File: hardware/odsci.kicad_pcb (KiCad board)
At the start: 4 copper layers, 50 x 69.2 mm, 29 parts, among them J1 USB_C_Receptacle, J2 Conn_01x03_Pin, J3 Conn_01x04_Pin, J4 Screw_Terminal_01x03, SW1 SW_Push, U1 TPS7A4701xRGW, U2 STM32F042K6Tx, U3 USBLC6-2SC6

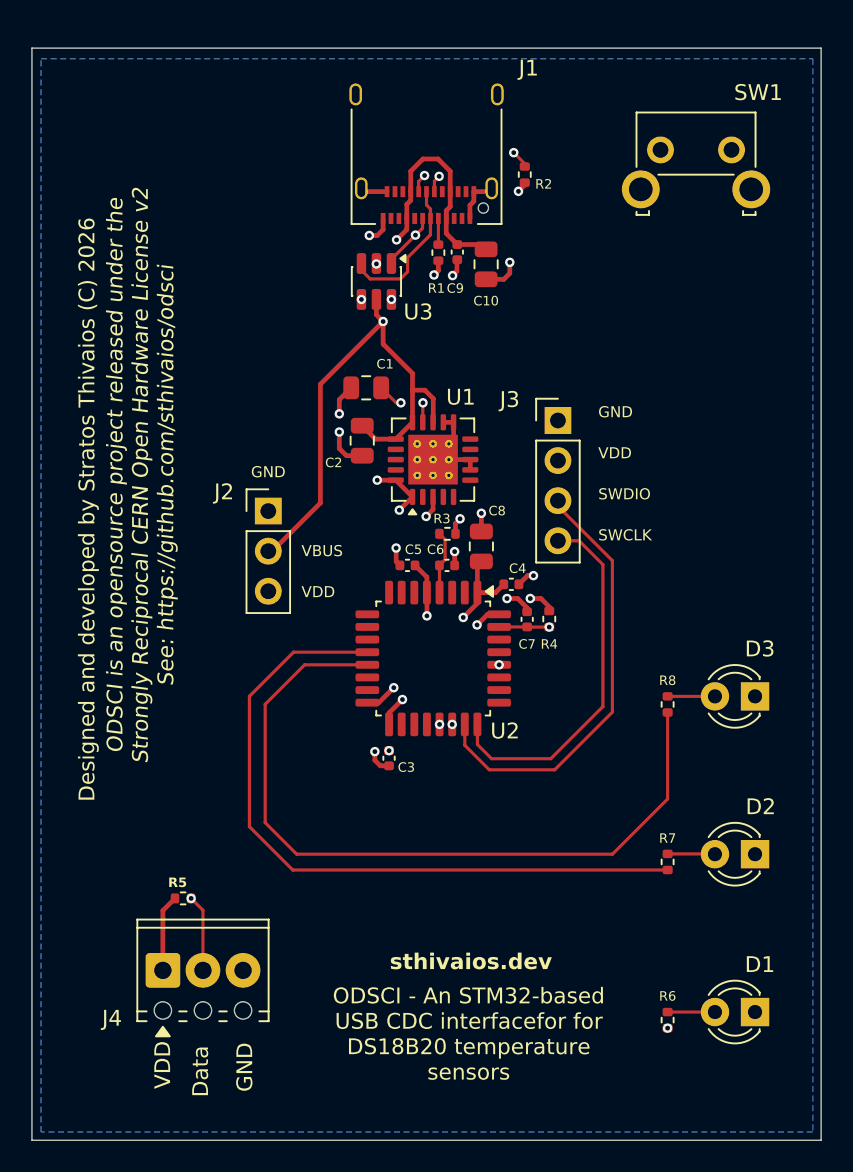
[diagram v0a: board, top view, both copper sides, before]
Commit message: hardware: add mounting holes to pcb
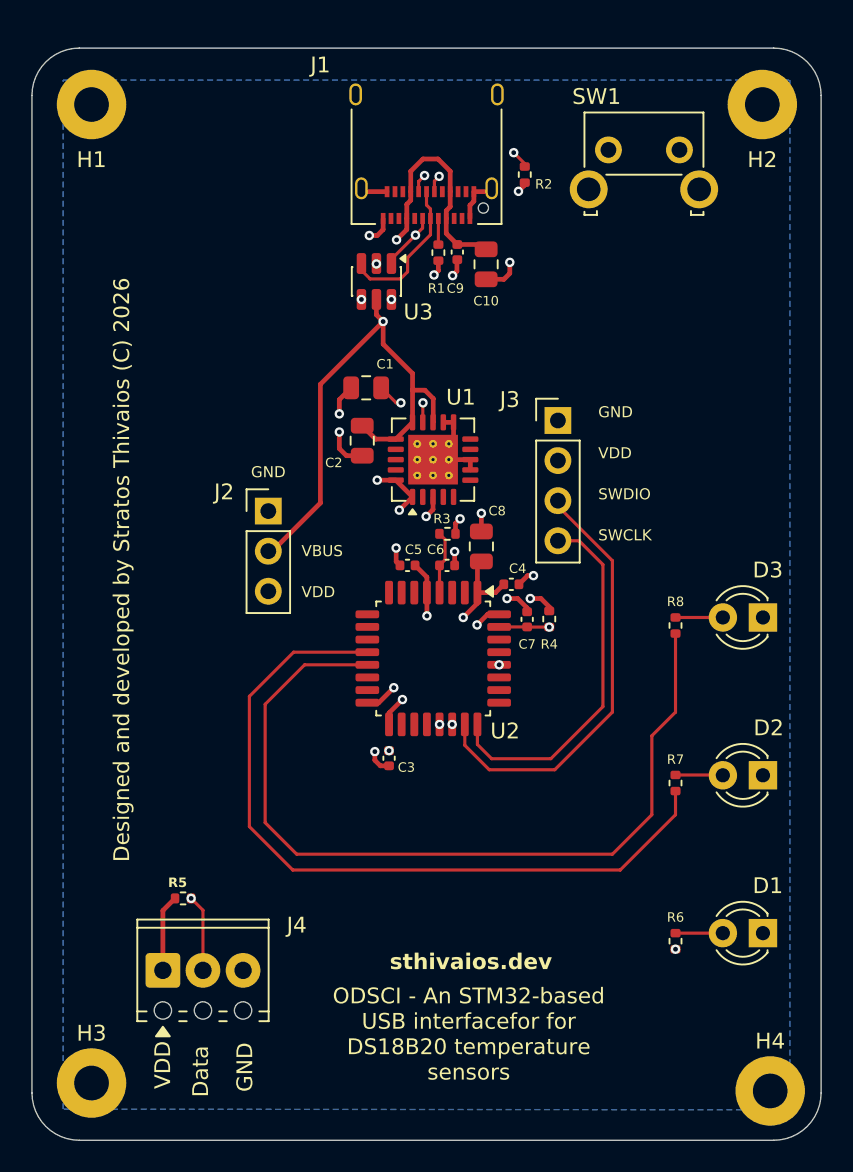
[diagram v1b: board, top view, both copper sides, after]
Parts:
- added H1: MountingHole_Pad, MountingHole:MountingHole_2.2mm_M2_Pad, F.Cu at (129.5, 75.5)
- added H2: MountingHole_Pad, MountingHole:MountingHole_2.2mm_M2_Pad, F.Cu at (172.0, 75.5)
- added H3: MountingHole_Pad, MountingHole:MountingHole_2.2mm_M2_Pad, F.Cu at (129.5, 137.5)
- added H4: MountingHole_Pad, MountingHole:MountingHole_2.2mm_M2_Pad, F.Cu at (172.5, 138.0)
- moved D1 5.02 mm to (172.0, 128.0)
- moved D2 5.02 mm to (172.0, 118.0)
- moved D3 5.02 mm to (172.0, 108.0)
- moved R6 5.02 mm to (166.5, 128.5)
- moved R7 5.02 mm to (166.5, 118.5)
- moved R8 5.02 mm to (166.5, 108.5)
- moved SW1 3.30 mm to (162.2, 78.4)
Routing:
- net CAPTURE_LED: track 48.3 -> 53.5 mm
- net ACTIVITY_LED: track 44.5 -> 48.0 mm
- net Net-(U2-PB8): track 38.2 -> 36.8 mm
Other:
- outline, holes or cut-outs redrawn
- board text added: "ODSCI - An STM32-based USB interfacefor for DS18B20 temperature sensors"
- board text removed: "ODSCI - An STM32-based USB CDC interfacefor for DS18B20 temperature sensors"
- board text removed: "ODSCI is an opensource project released under the Strongly Reciprocal CERN Open Hardware License v2 See: https://github.com/sthivaios/odsci"

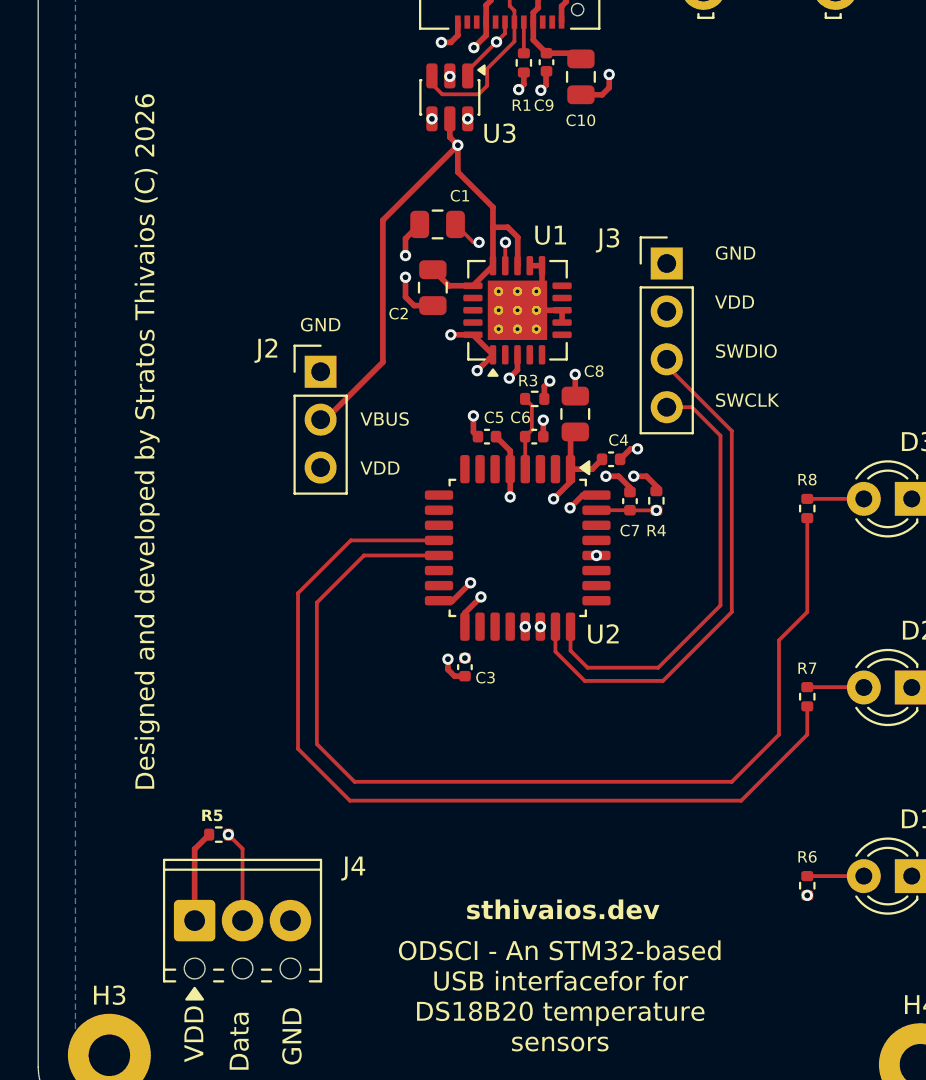
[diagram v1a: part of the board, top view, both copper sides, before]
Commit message: hardware: add a few decoupling caps
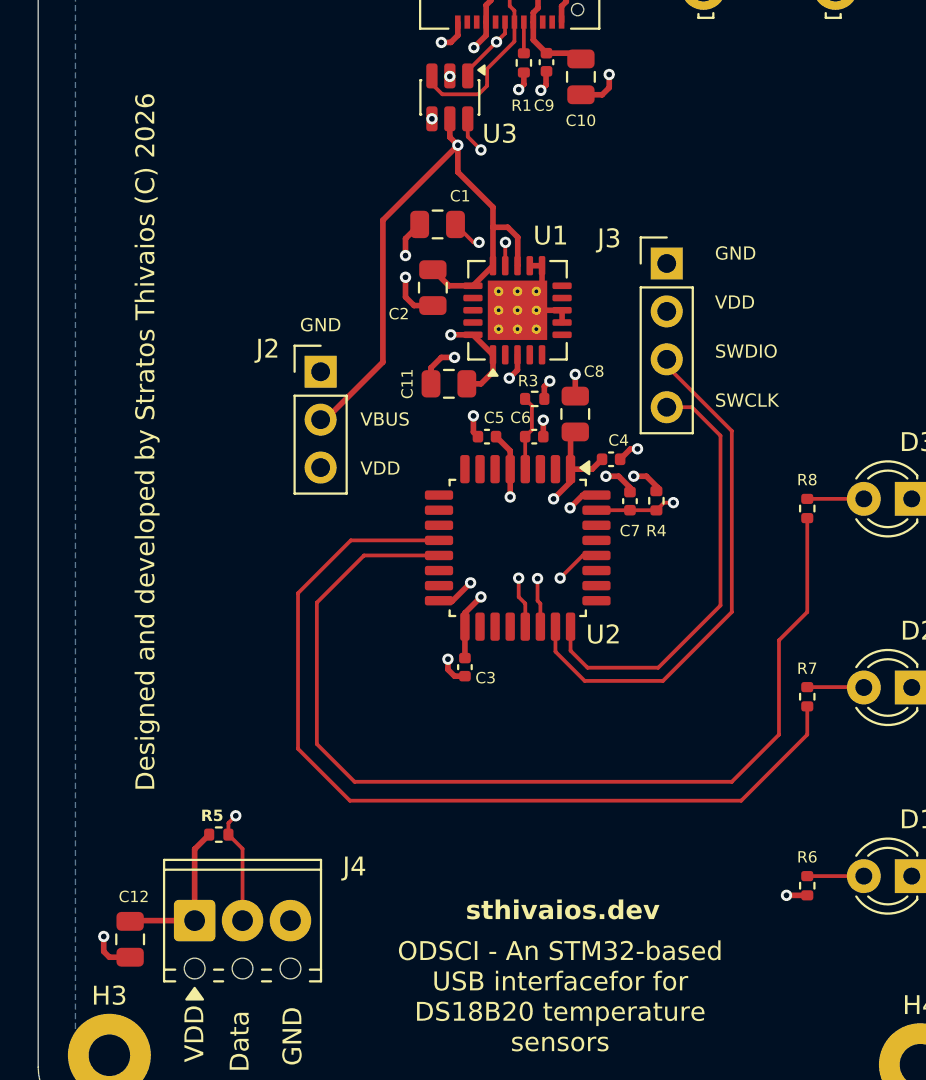
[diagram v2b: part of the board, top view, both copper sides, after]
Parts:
- added C11: 47uF, Capacitor_SMD:C_0805_2012Metric, F.Cu at (147.5, 101.9)
- added C12: 4.7uF, Capacitor_SMD:C_0805_2012Metric, F.Cu at (130.6, 131.3)
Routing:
- net VDD: track 23.1 -> 30.8 mm, vias 9 -> 7
- net GND: track 33.6 -> 38.3 mm, vias 17 -> 19
- net ONEWIRE_BUS: track 34.3 -> 37.8 mm
- net USB_D_POSITIVE: track 35.0 -> 35.6 mm
- net USB_D_NEGATIVE: track 31.9 -> 32.5 mm

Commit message: hardware: layout of pcb
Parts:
- moved C12 60.7 mm to (191.0, 125.8)
- moved J4 60.7 mm to (194.5, 124.8)
- moved R5 60.7 mm to (195.7, 120.2)
- moved H3 58.6 mm to (187.6, 130.1)
- moved H1 58.5 mm to (187.8, 70.2)
- moved C1 57.3 mm to (203.8, 86.6)
- moved C10 57.3 mm to (211.4, 78.8)
- moved C11 57.3 mm to (204.4, 95.1)
- moved C2 57.3 mm to (203.6, 90.0)
- moved C3 57.3 mm to (205.3, 110.1)
- moved C4 57.3 mm to (213.0, 99.1)
- moved C5 57.3 mm to (206.4, 97.9)
- moved C6 57.3 mm to (208.9, 97.9)
- moved C7 57.3 mm to (214.0, 101.3)
- moved C8 57.3 mm to (211.1, 96.7)
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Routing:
- net ONEWIRE_BUS: track 37.8 -> 34.0 mm
- net Net-(U2-PB8): track 37.1 -> 35.6 mm
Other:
- board size 50 x 69.2 mm -> 50 x 70 mm

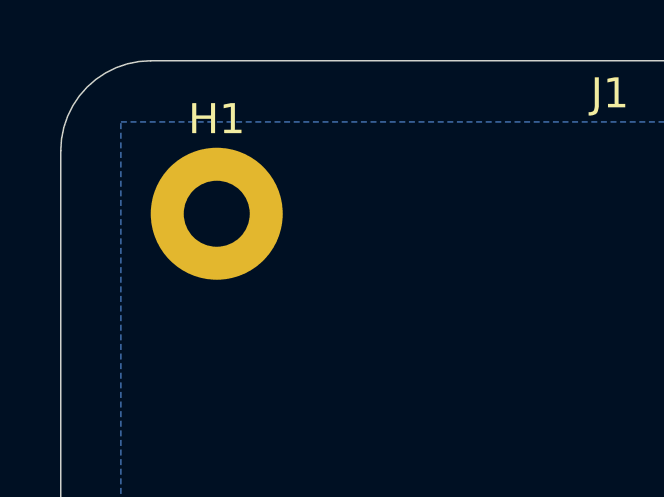
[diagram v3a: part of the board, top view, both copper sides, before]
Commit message: hardware: fix mounting hole positions
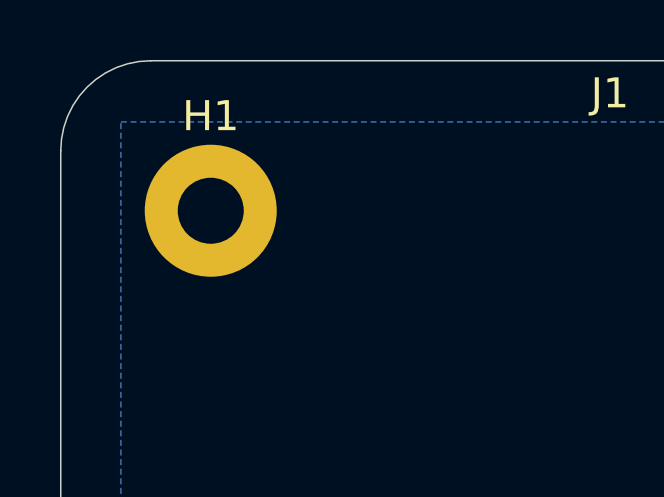
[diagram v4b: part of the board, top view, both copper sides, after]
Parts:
- moved H1 0.22 mm to (187.6, 70.1)
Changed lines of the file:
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@@
 	(footprint "MountingHole:MountingHole_2.2mm_M2_Pad"
 		(layer "F.Cu")
-		(at 187.8 70.2)
+		(at 187.6 70.100001)
 		(descr "Mounting Hole 2.2mm, M2, generated by kicad-footprint-generator mountinghole.py")
 		(tags "mountinghole M2")

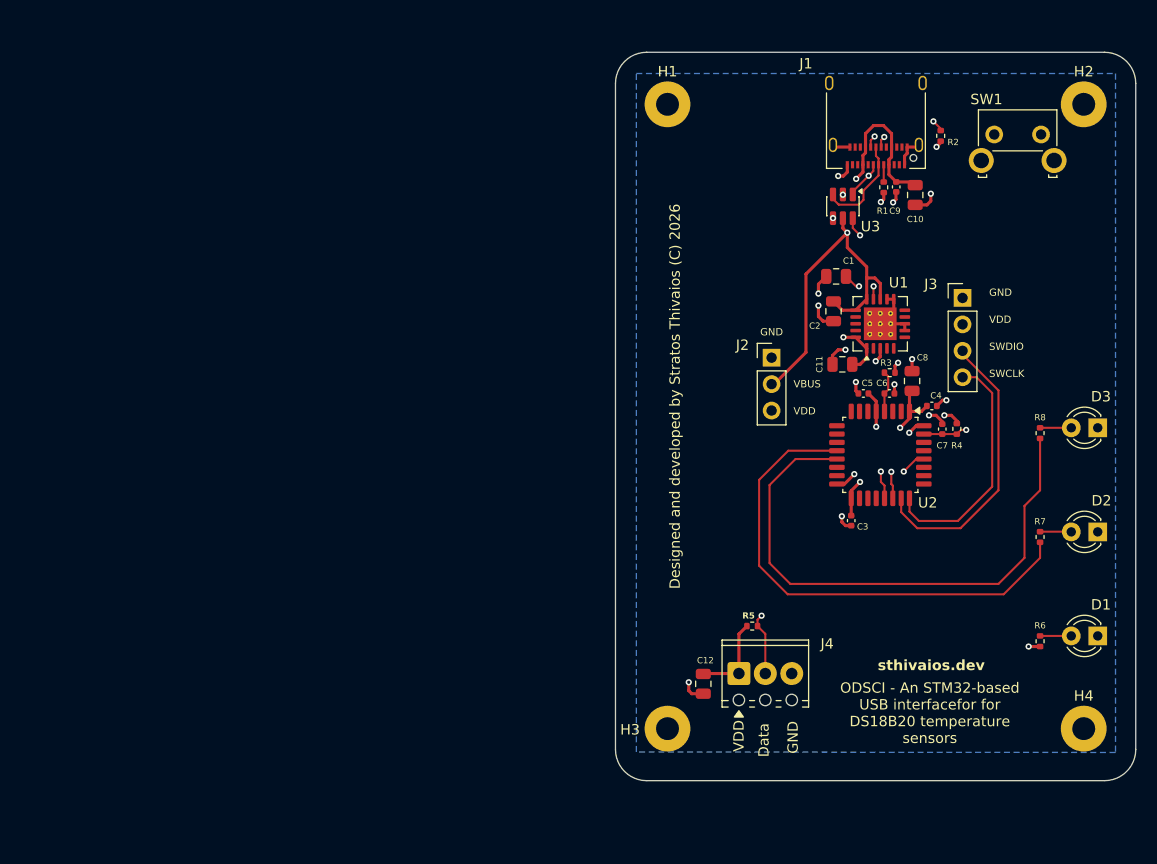
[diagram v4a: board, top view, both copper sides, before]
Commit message: hardware: fully reroute and change pcb's layout
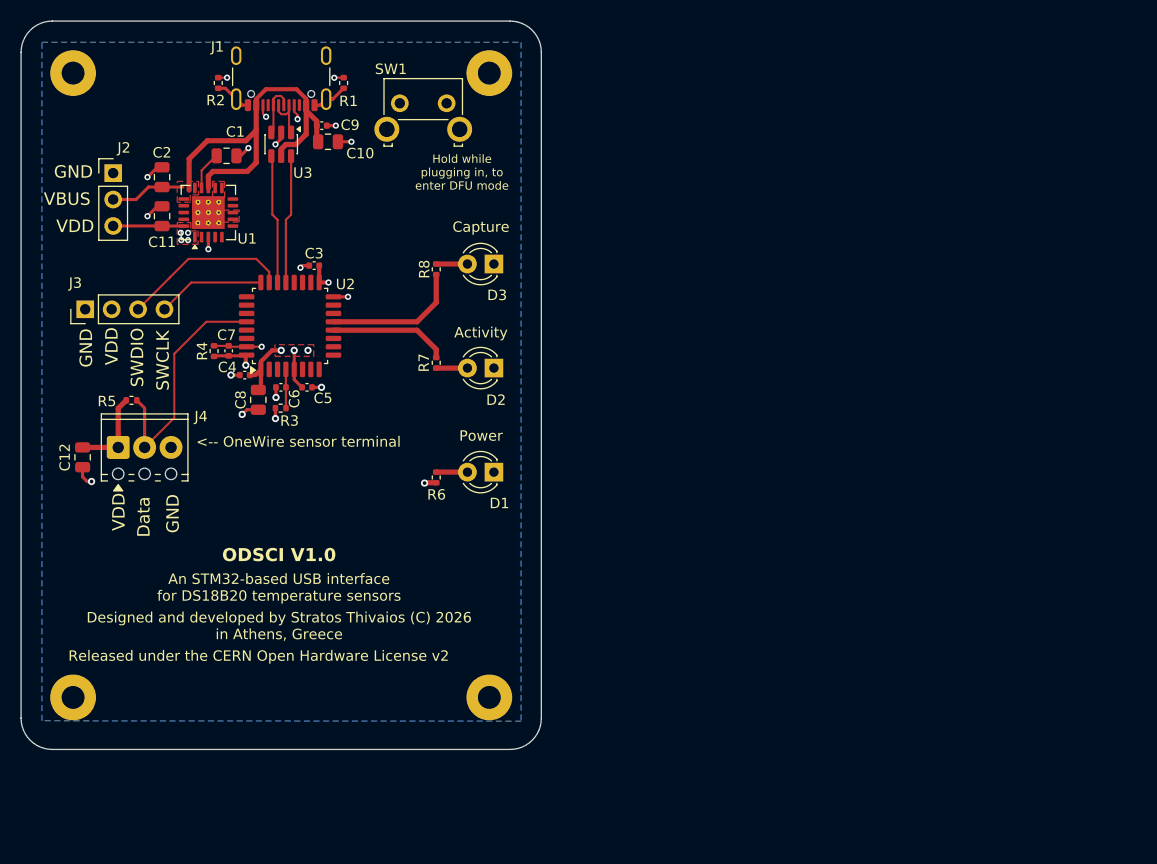
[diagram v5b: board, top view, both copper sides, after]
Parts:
- J1: footprint Connector_USB:USB_C_Receptacle_Amphenol_12401610E4-2A -> Connector_USB:USB_C_Receptacle_GCT_USB4105-xx-A_16P_TopMnt_Horizontal
- moved J3 84.3 mm to (131.6, 89.8), turned to 90 degrees
- moved R4 71.8 mm to (144.0, 93.8), turned to -90 degrees
- moved R2 69.6 mm to (144.4, 68.0)
- moved C7 69.0 mm to (145.4, 93.8), turned to -90 degrees
- moved C11 66.9 mm to (139.0, 80.8), turned to 90 degrees
- moved C4 66.1 mm to (147.0, 96.1), turned to 0 degrees
- moved C2 65.8 mm to (139.0, 77.1), turned to -90 degrees
- moved J2 65.7 mm to (134.3, 76.7)
- moved U1 65.4 mm to (143.5, 80.5)
- moved C12 63.5 mm to (131.4, 104.0)
- moved J4 63.5 mm to (134.8, 103.1)
- moved R5 63.5 mm to (136.1, 98.5)
- moved C8 62.9 mm to (148.3, 98.5), turned to 90 degrees
- moved R7 60.4 mm to (165.4, 94.9), turned to 90 degrees
- moved R6 60.1 mm to (165.4, 106.0)
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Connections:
- J1 pad A8: unconnected-(J1-SBU1-PadA8) -> (no net)
- J1 pad B8: unconnected-(J1-SBU2-PadB8) -> (no net)
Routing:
- net CAPTURE_LED: track 53.5 -> 13.5 mm
- net ACTIVITY_LED: track 48.0 -> 11.4 mm
- net USB_D_POSITIVE: track 35.6 -> 12.4 mm, vias 2 -> 0
- net USB_D_NEGATIVE: track 32.5 -> 12.4 mm, vias 2 -> 0
- net VDD: track 30.8 -> 46.4 mm, vias 7 -> 11
- net SWCLK_PA14: track 23.4 -> 10.3 mm
- net VBUS: track 58.6 -> 46.8 mm, vias 2 -> 0
- net SWDIO_PA13: track 27.7 -> 16.2 mm
- net ONEWIRE_BUS: track 34.0 -> 23.2 mm, vias 2 -> 0
- net GND: track 38.3 -> 28.7 mm, vias 19 -> 14
- net Net-(J1-CC1): track 1.66 -> 9.22 mm, vias 0 -> 2
- net Net-(J1-D+-PadA6): track 9.55 -> 5.14 mm
- net Net-(J1-D--PadA7): track 9.11 -> 5.14 mm, vias 2 -> 0
- net Net-(U2-PB8): track 35.6 -> 39.2 mm
- net Net-(U1-NR): track 4.29 -> 3.74 mm, vias 2 -> 0
- added copper zone on F.Cu, net GND
- added copper zone on F.Cu, net VBUS
- added copper zone on F.Cu, net VDD
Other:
- board text added: "<-- OneWire sensor terminal"
- board text added: "Activity"
- board text added: "An STM32-based USB interface for DS18B20 temperature sensors"
- board text added: "Capture"
- board text added: "Designed and developed by Stratos Thivaios (C) 2026 in Athens, Greece"
- board text added: "Hold while plugging in, to enter DFU mode"
- board text added: "ODSCI V1.0"
- board text added: "Power"
- board text added: "Released under the CERN Open Hardware License v2"
- board text removed: "Designed and developed by Stratos Thivaios (C) 2026"
- board text removed: "ODSCI - An STM32-based USB interfacefor for DS18B20 temperature sensors"
- board text removed: "sthivaios.dev"
